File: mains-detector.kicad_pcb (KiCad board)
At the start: 4 copper layers, 52.2 x 30.8 mm, 53 parts, among them J2 FS1000A, J3 GPIOS, J4 ANT, Q1 IRLML2402, Q2 IRLML2402, SW1 RESET, SW2 ONOFF, U1 XC6206P332PR-G, U2 TP4065-4.2V-SOT25-R, U3 NE555D

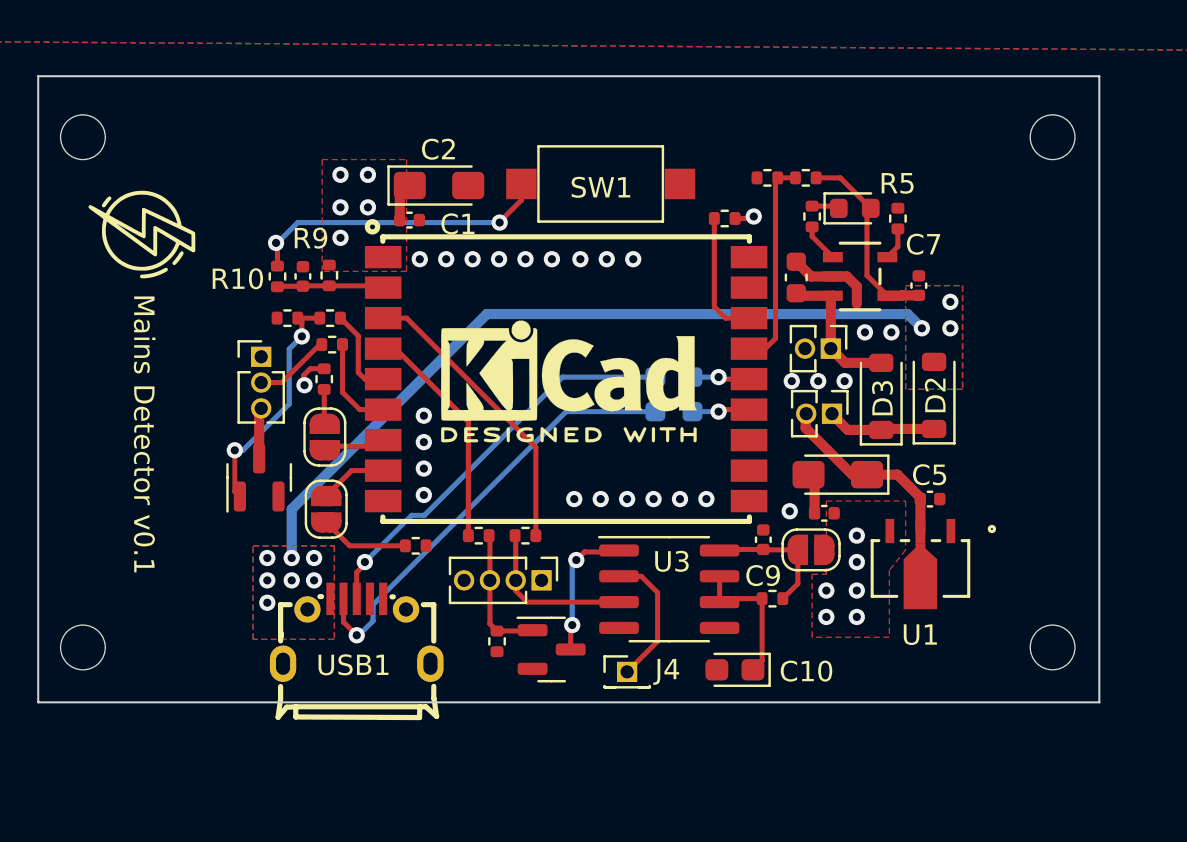
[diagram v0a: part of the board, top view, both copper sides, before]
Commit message: Fix schematic / pcb design gaps, update enclosure
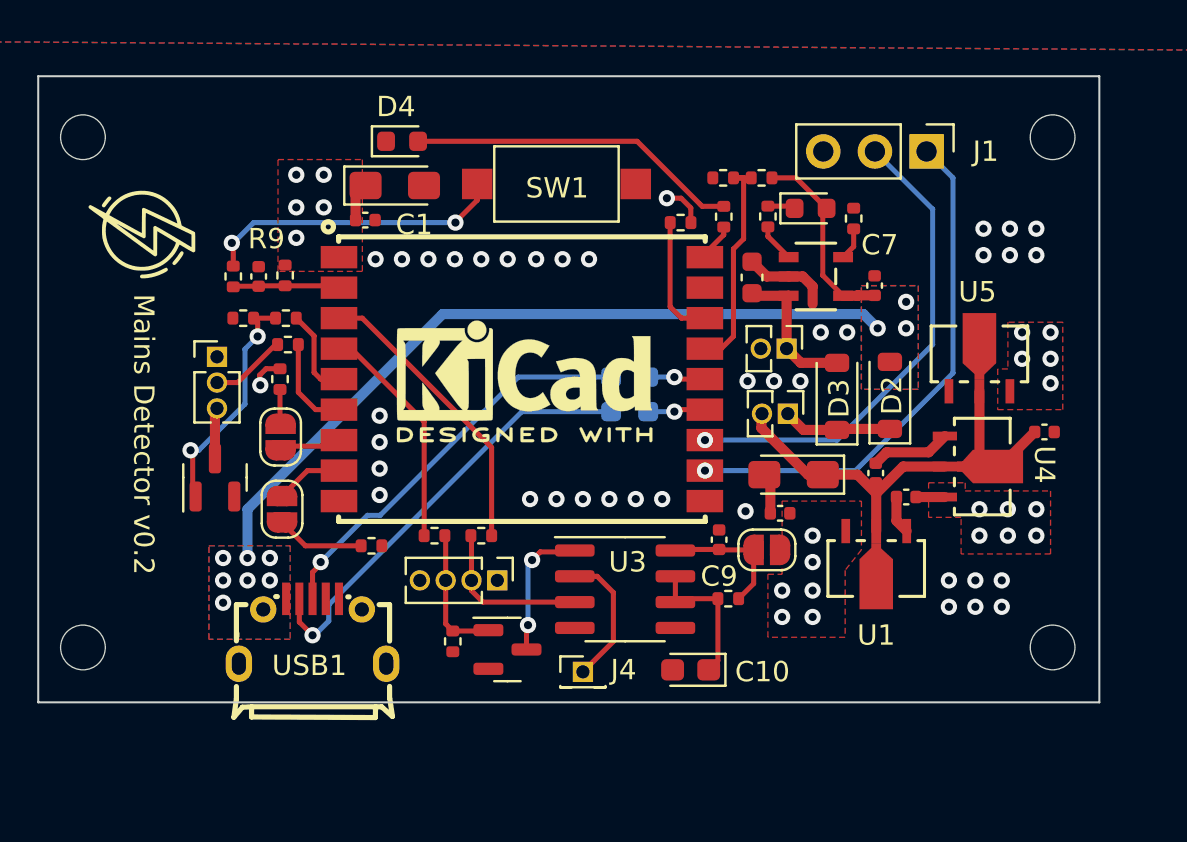
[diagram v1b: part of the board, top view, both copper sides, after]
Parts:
- added C11: 1u, Capacitor_SMD:C_0402_1005Metric, F.Cu at (49.5, 17.5)
- added C12: 1u, Capacitor_SMD:C_0402_1005Metric, F.Cu at (42.7, 20.7)
- added D4: STATUS, LED_SMD:LED_0603_1608Metric, F.Cu at (17.9, 3.20)
- added J1: UART, Connector_PinHeader_2.54mm:PinHeader_1x03_P2.54mm_Vertical, F.Cu at (43.7, 3.70)
- added R8: 3k, Resistor_SMD:R_0402_1005Metric, F.Cu at (33.7, 6.91)
- added U4: XC6206P332PR-G, footprints:SOT-89_TOR, F.Cu at (46.4, 19.2)
- added U5: XC6206P332PR-G, footprints:SOT-89_TOR, F.Cu at (46.3, 13.7)
- R6: value 10k -> 5k
- moved C5 2.96 mm to (41.2, 19.5), turned to 90 degrees
- moved R1 2.18 mm to (31.6, 7.20)
- moved BT1 2.18 mm to (36.8, 13.4)
- moved C10 2.18 mm to (32.1, 29.2)
- moved C4 2.18 mm to (37.2, 19.6)
- moved C6 2.18 mm to (36.5, 21.5)
- moved C9 2.18 mm to (33.5, 22.8)
- moved D1 2.18 mm to (38.0, 6.50)
- moved JP3 2.18 mm to (35.8, 23.3)
- moved U2 2.18 mm to (38.3, 9.85)
- moved C1 2.18 mm to (16.1, 7.08)
- moved J2 2.18 mm to (8.79, 13.8)
- moved J3 2.18 mm to (22.6, 24.8)
- moved JP2 2.18 mm to (12.0, 21.3)
- moved Q1 2.18 mm to (23.1, 28.2)
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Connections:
- L1 pad 11: unconnected-(L1-RXD-Pad11) -> Net-(J1-Pin_1)
- L1 pad 12: unconnected-(L1-TXD-Pad12) -> Net-(J1-Pin_2)
- L1 pad 18: unconnected-(L1-IO0-Pad18) -> Net-(L1-IO0)
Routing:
- net Net-(J1-Pin_1): track 0.00 -> 25.6 mm, vias 0 -> 1
- net Net-(J1-Pin_2): track 0.00 -> 23.8 mm, vias 0 -> 1
- net Net-(D4-A): track 0.00 -> 16.4 mm
- net Net-(SW2-B): track 9.42 -> 21.2 mm
- net GND: track 6.37 -> 12.2 mm, vias 25 -> 37
- net VCC: track 4.49 -> 6.85 mm, vias 13 -> 24
- net Net-(L1-IO0): track 0.00 -> 1.87 mm
- net SENSE: track 10.3 -> 11.0 mm
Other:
- board text added: "Mains Detector v0.2"
- board text removed: "Mains Detector v0.1"
